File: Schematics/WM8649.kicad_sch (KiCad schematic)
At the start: 6 parts, among them J10 Line In, J11 BOB21250-LEFT, J12 BOB21250-RIGHT, J9 Line In

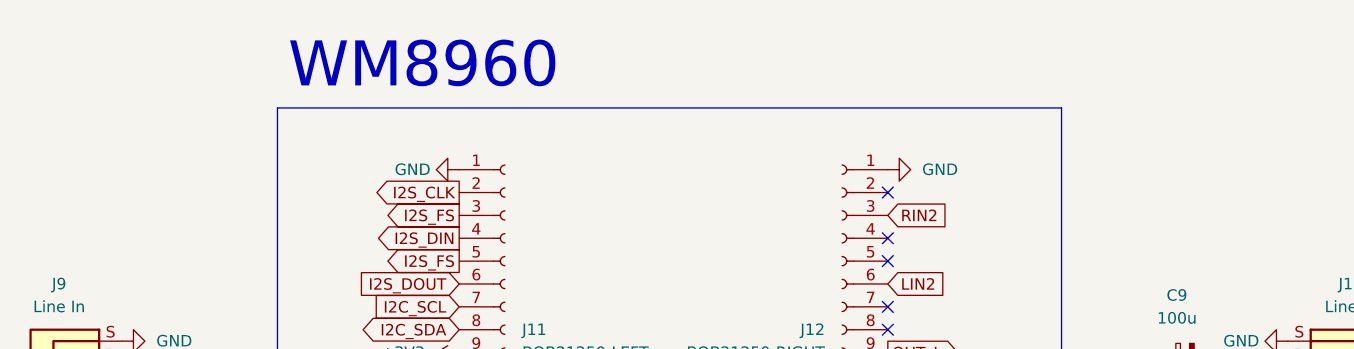
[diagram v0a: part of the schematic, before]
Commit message: Finished PCB routing
New Layout fits perfectly, now all the parts are through-hole and routed together. 20 Vias is a nightmare but better than what we started with
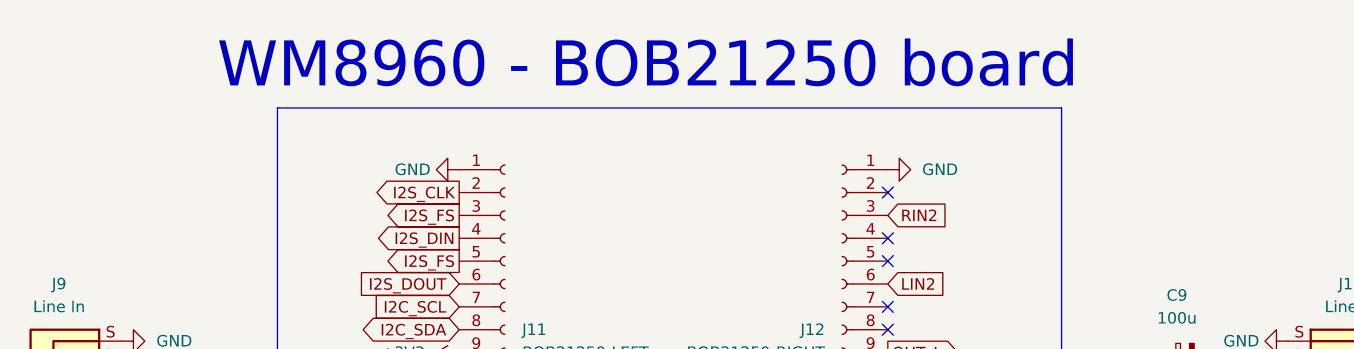
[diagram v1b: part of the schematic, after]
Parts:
- C13, C9: footprint (none) -> Capacitor_THT:CP_Radial_D8.0mm_P5.00mm
- J11, J12: footprint (none) -> Connector_PinSocket_2.54mm:PinSocket_1x16_P2.54mm_Vertical
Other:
- note added: "WM8960 - BOB21250 board"
- note removed: "WM8960"
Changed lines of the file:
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@@
 		)
 	)
-	(text "WM8960"
-		(exclude_from_sim no)
-		(at 114.808 67.31 0)
+	(text "WM8960 - BOB21250 board"
+		(exclude_from_sim no)
+		(at 139.7 67.31 0)
 		(effects
 			(font
@@
 			)
 		)
-		(property "Footprint" ""
+		(property "Footprint" "Capacitor_THT:CP_Radial_D8.0mm_P5.00mm"
 			(at 209.55 101.9048 0)
 			(effects
@@
 			)
 		)
-		(property "Footprint" ""
+		(property "Footprint" "Connector_PinSocket_2.54mm:PinSocket_1x16_P2.54mm_Vertical"
 			(at 123.825 96.52 0)
 			(effects
@@
 			)
 		)
-		(property "Footprint" ""
+		(property "Footprint" "Capacitor_THT:CP_Radial_D8.0mm_P5.00mm"
 			(at 203.2 99.3648 0)
 			(effects
@@
 			)
 		)
-		(property "Footprint" ""
+		(property "Footprint" "Connector_PinSocket_2.54mm:PinSocket_1x16_P2.54mm_Vertical"
 			(at 161.29 96.52 0)
 			(effects

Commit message: File labelling
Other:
- note added: "Drawn by Harvey McBurney, Nicolas Viale"
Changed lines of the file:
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@@
+		)
+	)
+	(text "Drawn by Harvey McBurney, Nicolas Viale"
+		(exclude_from_sim no)
+		(at 209.804 169.672 0)
+		(effects
+			(font
+				(size 2 2)
+				(thickness 0.6)
+				(bold yes)
+			)
 		)
 	)

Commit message: Tidied up Schematic
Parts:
- J10: value Line In -> Line Out
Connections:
- net OUT_L: no longer C13.1
- net OUT_R: now also C13.1
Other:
- note added: "Caps mean sleeve can be grounded as opposed to connecting to OUT3"
- note removed: "WM8960 - BOB21250 board"
- moved on the sheet: C13, C9, J10, J9

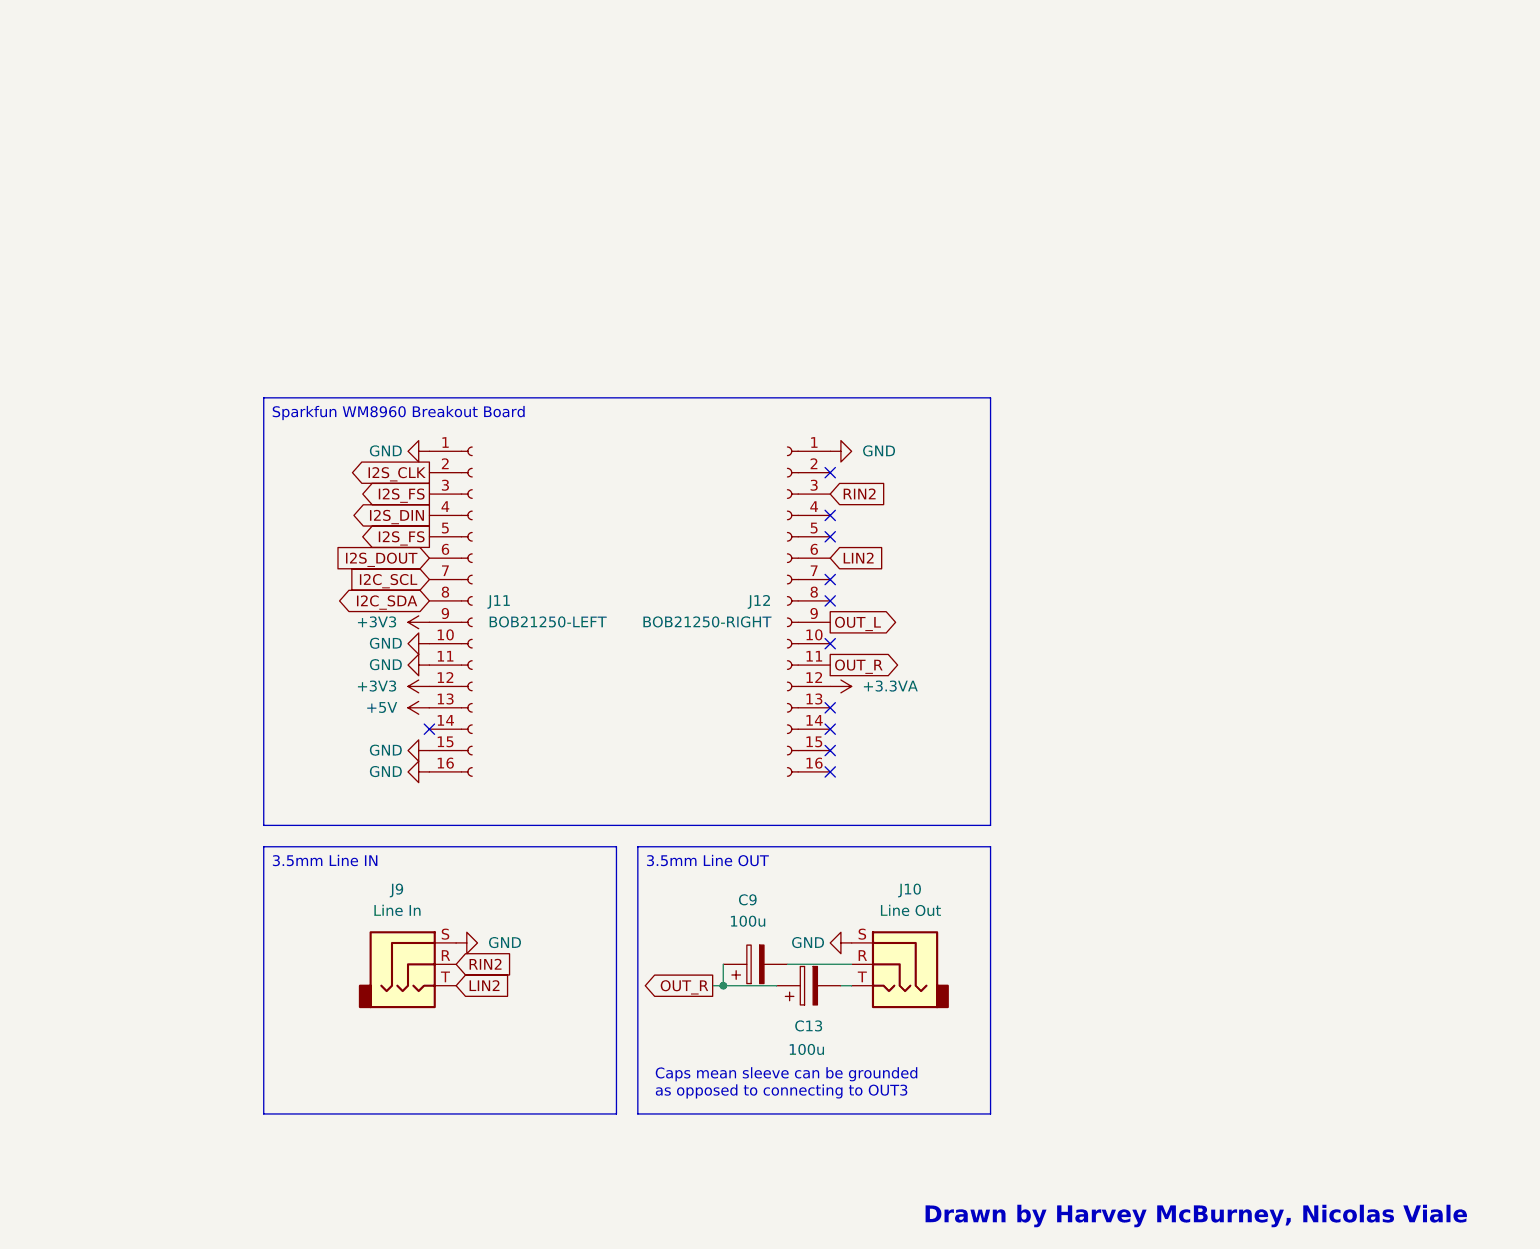
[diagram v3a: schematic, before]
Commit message: Fixed power connections on CODEC
So the codec board regulates its own AVDD which we had named but disconnected. In order for this regulation to happen the EN pin must be pulled high (not low as it says in the documentation).
SPKVDD was also disconnected as by default this is taken from VIN (5V) anyway, this means the CODEC boards don't need to be modified anymore.
Still need to test these on the board if time allows.
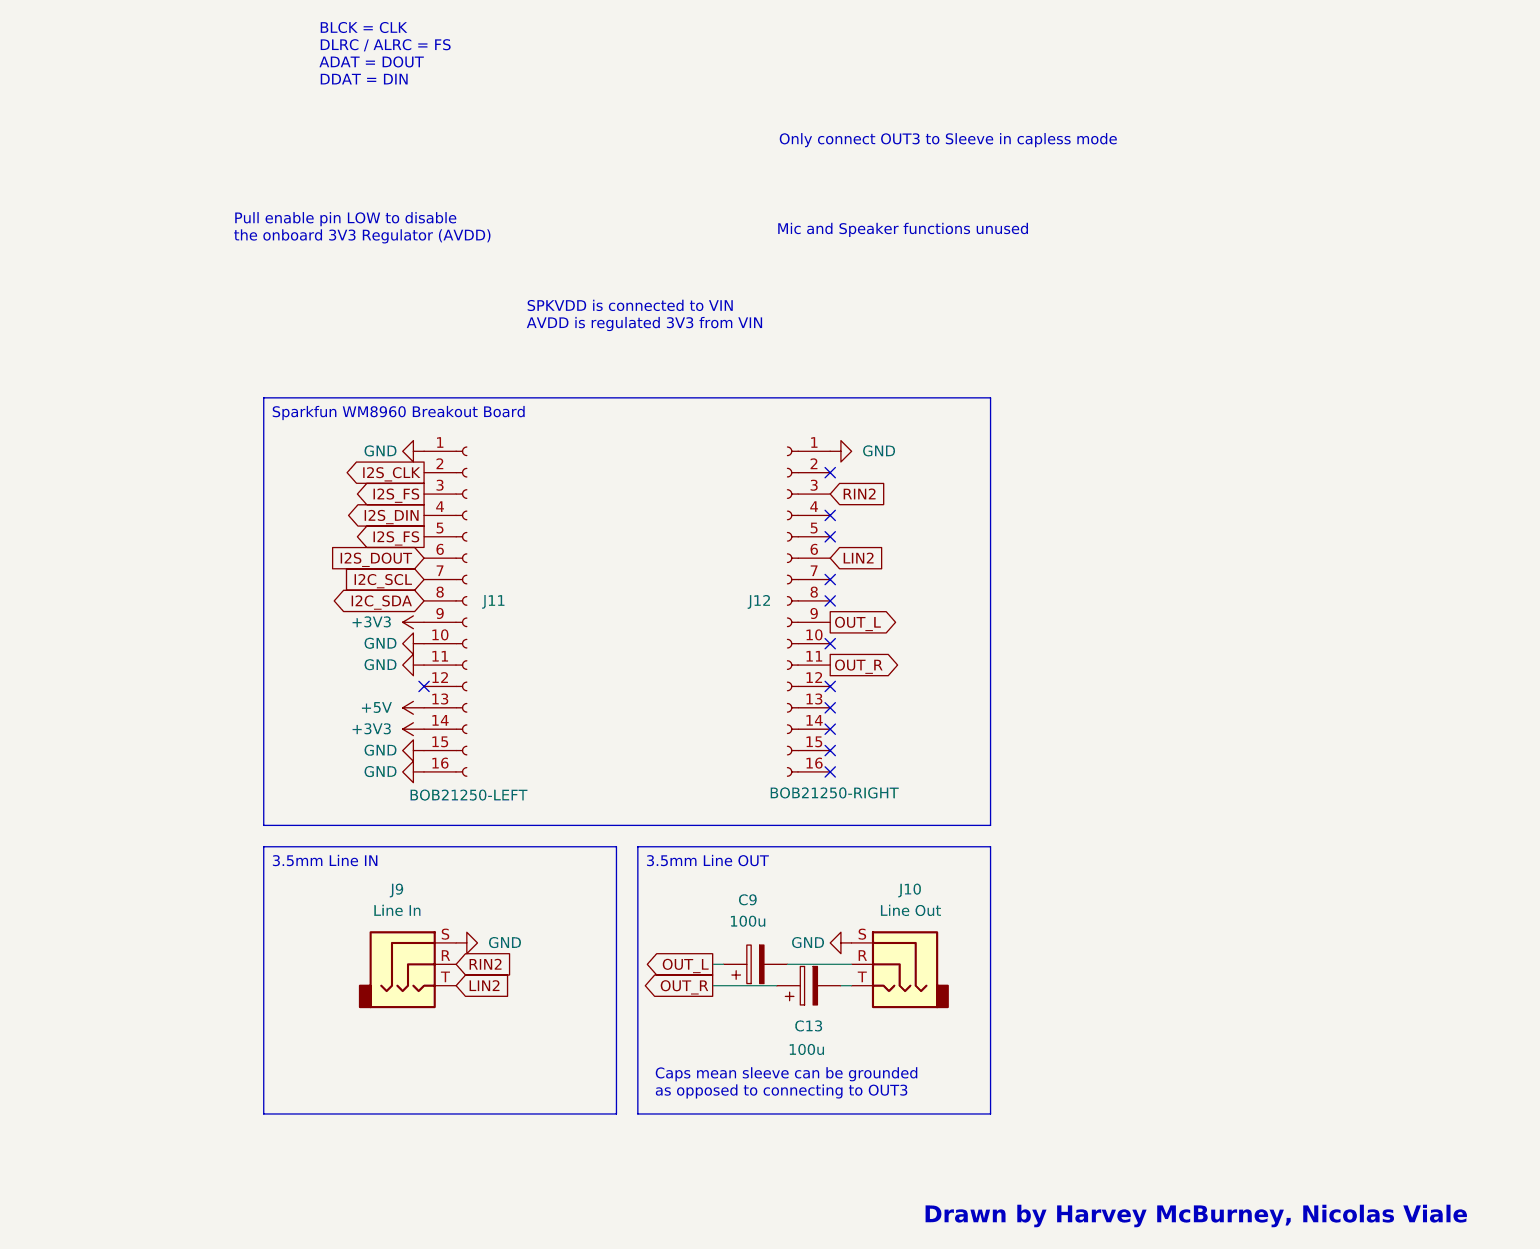
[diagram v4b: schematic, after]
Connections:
- net +3V3: now also J11.14 (Pin_14); no longer J11.12 (Pin_12)
- net OUT_L: now also C9.1
- net OUT_R: no longer C9.1
- net +3.3VA: no longer names the net of J12.12 (Pin_12)
- no-connect marks 11 -> 12
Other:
- note added: "BLCK = CLK DLRC / ALRC = FS ADAT = DOUT DDAT = DIN"
- note added: "Mic and Speaker functions unused"
- note added: "Only connect OUT3 to Sleeve in capless mode"
- note added: "Pull enable pin LOW to disable the onboard 3V3 Regulator (AVDD)"
- note added: "SPKVDD is connected to VIN AVDD is regulated 3V3 from VIN"
- moved on the sheet: J11

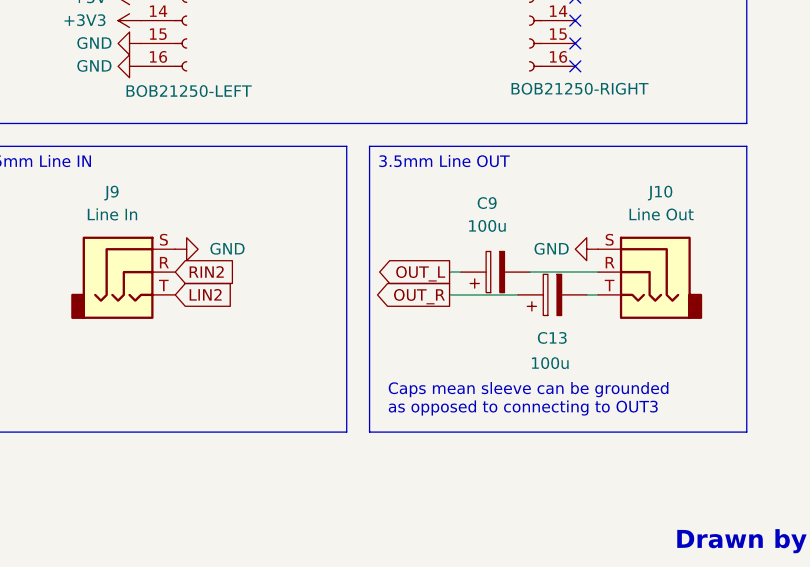
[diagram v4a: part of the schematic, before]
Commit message: Fixed left and right output channels
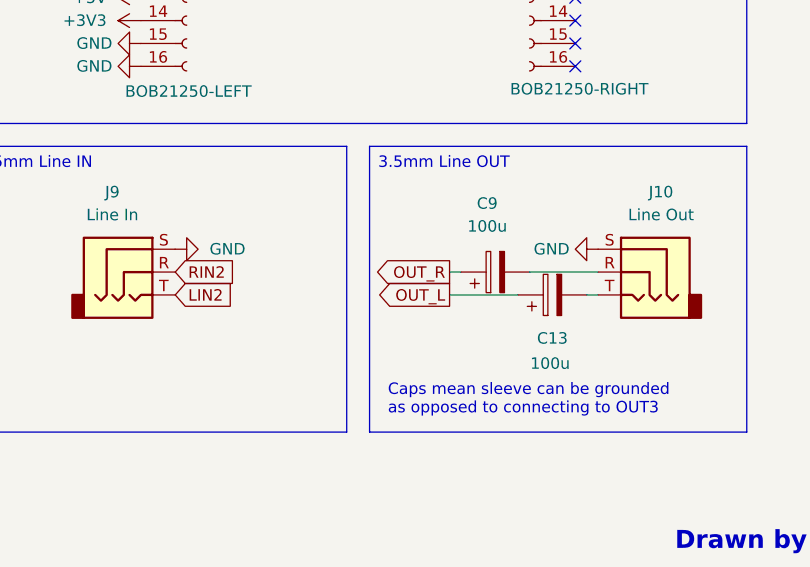
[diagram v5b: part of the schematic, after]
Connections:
- net OUT_L: now also C13.1; no longer C9.1
- net OUT_R: now also C9.1; no longer C13.1
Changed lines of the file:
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@@
 		)
 	)
-	(global_label "OUT_L"
+	(global_label "OUT_R"
 		(shape output)
 		(at 152.4 139.7 180)
@@
 		)
 		(property "Intersheetrefs" "${INTERSHEET_REFS}"
-			(at 143.7905 139.7 0)
+			(at 143.5486 139.7 0)
 			(effects
 				(font
@@
 		)
 	)
-	(global_label "OUT_R"
+	(global_label "OUT_L"
 		(shape output)
 		(at 152.4 142.24 180)
@@
 		)
 		(property "Intersheetrefs" "${INTERSHEET_REFS}"
-			(at 143.5486 142.24 0)
+			(at 143.7905 142.24 0)
 			(effects
 				(font
